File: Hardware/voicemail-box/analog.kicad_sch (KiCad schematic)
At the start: 0 parts

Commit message: ~working on first pcb-Draft
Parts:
- added C25, C26, C29: 10u, Capacitor_SMD:C_0201_0603Metric_Pad0.64x0.40mm_HandSolder, symbol Device:C
- added C27, C28: 1u, Capacitor_SMD:C_0201_0603Metric_Pad0.64x0.40mm_HandSolder, symbol Device:C
- added J2, J7: Conn_02x04_Odd_Even, Connector_PinHeader_2.54mm:PinHeader_2x04_P2.54mm_Vertical, symbol Connector_Generic:Conn_02x04_Odd_Even
- added J3: AudioJack4_SwitchT1, Connector_Audio:Jack_3.5mm_CUI_SJ1-3515N_Horizontal, symbol Connector_Audio:AudioJack4_SwitchT1
- added J4: AudioJack3_Ground, Connector_Audio:Jack_3.5mm_CUI_SJ-3524-SMT_Horizontal, symbol Connector_Audio:AudioJack3_Ground
- added RN4, RN5: 10k, Resistor_SMD:R_Array_Convex_4x0603, symbol Device:R_Pack04
- added U3: PCM5122PW, Package_SO:TSSOP-28_4.4x9.7mm_P0.65mm, symbol Audio:PCM5122PW
- added U4: PCM1809, myParts:WQFN-20-1EP_3x3mm_P0.4mm_EP1.7x1.7mm, symbol myParts:pcm1809
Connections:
- new net: C29.1, U4.17 (AREG)
- new net: C28.1, U4.18 (VREF)
- new net: J2.2 (Pin_2), RN4.5 (R4.2), U4.11 (MD1)
- new net: J2.4 (Pin_4), RN4.6 (R3.2), U4.12 (MD0)
- new net: J2.6 (Pin_6), RN4.7 (R2.2), U4.13 (MSZ)
- new net: J2.8 (Pin_8), RN4.8 (R1.2), U4.19 (FMT0)
- new net: C25.1, U4.14 (DREG)
- new net: C26.1, U4.9 (IOVDD)
- new net: J7.2 (Pin_2), RN5.5 (R4.2), U3.15 (GPIO3/AGNS)
- new net: J7.4 (Pin_4), RN5.6 (R3.2), U3.14 (GPIO4/MAST)
- new net: J7.6 (Pin_6), RN5.7 (R2.2), U3.13 (GPIO5/ATT0)
- new net: J7.8 (Pin_8), RN5.8 (R1.2), U3.19 (GPIO6/FLT)
- new net +3V3: C27.1, RN4.1 (R1.1), RN4.2 (R2.1), RN4.3 (R3.1), RN4.4 (R4.1), RN5.1 (R1.1), RN5.2 (R2.1), RN5.3 (R3.1), RN5.4 (R4.1), U4.16 (AVDD)
- new net ADC_I2S_BCLK: U4.7 (BCLK)
- new net ADC_I2S_FSYNC: U4.8 (FSYNC)
- new net ADC_I2S_SDOUT: U4.6 (SDOUT)
- new net GND: C25.2, C26.2, C27.2, C28.2, C29.2, J2.1 (Pin_1), J2.3 (Pin_3), J2.5 (Pin_5), J2.7 (Pin_7), J7.1 (Pin_1), J7.3 (Pin_3), J7.5 (Pin_5), J7.7 (Pin_7), U4.10 (VSS), U4.15 (VSS), U4.20 (VSS), U4.21 (VSS), U4.5 (VSS)
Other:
- note added: "DAC"
- note added: "Set Jumper for Cntr Signal Low"
- note added: "Signal from Tip Back (Phone Standard): - Left Audio - Right Audio - Ground - Microphone"

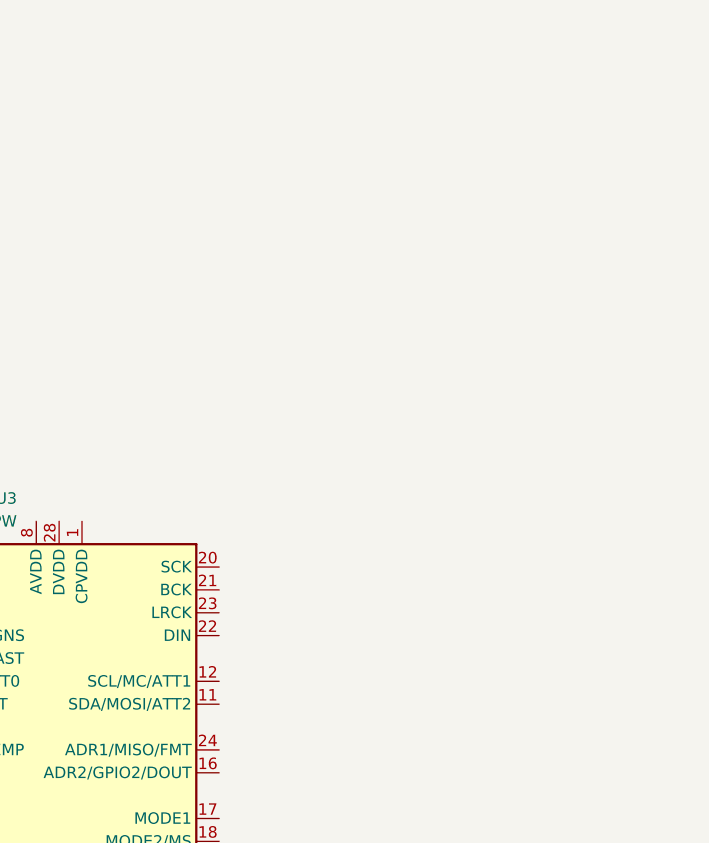
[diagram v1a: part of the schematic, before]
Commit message: - unused datasheets + new datasheets
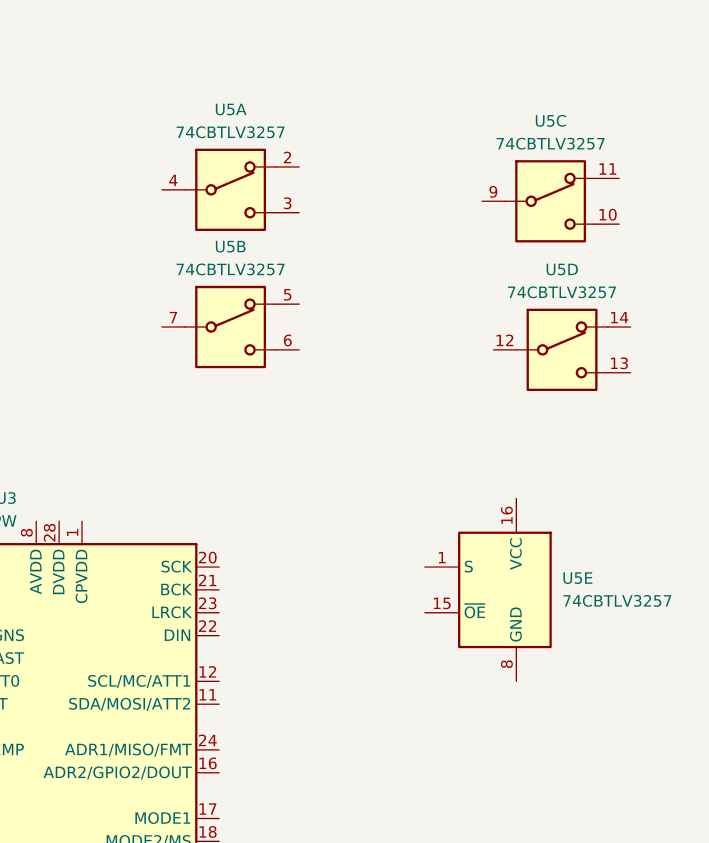
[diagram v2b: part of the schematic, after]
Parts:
- added U5: 74CBTLV3257, symbol 74xx:74CBTLV3257

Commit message: -
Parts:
- removed J2, J7: Conn_02x04_Odd_Even, Connector_PinHeader_2.54mm:PinHeader_2x04_P2.54mm_Vertical, symbol Connector_Generic:Conn_02x04_Odd_Even
- removed RN4, RN5: 10k, Resistor_SMD:R_Array_Convex_4x0603, symbol Device:R_Pack04
- removed U3: PCM5122PW, Package_SO:TSSOP-28_4.4x9.7mm_P0.65mm, symbol Audio:PCM5122PW
- removed U4: PCM1809, myParts:WQFN-20-1EP_3x3mm_P0.4mm_EP1.7x1.7mm, symbol myParts:pcm1809
- removed U5: 74CBTLV3257, symbol 74xx:74CBTLV3257
- added U3: TLV320AIC3104, Package_DFN_QFN:VQFN-32-1EP_5x5mm_P0.5mm_EP3.1x3.1mm, symbol myParts:TLV320AIC3104
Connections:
- net +3V3: no longer C27.1
- net GND: no longer C25.2, C26.2, C27.2, C28.2, C29.2
- new net CODEC_I2C_SCL: U3.8 (SCL)
- new net CODEC_I2C_SDA: U3.9 (SDA)
- new net CODEC_I2S_BCLK: U3.2 (BCLK)
- new net CODEC_I2S_DIN: U3.4 (DIN)
- new net CODEC_I2S_DOUT: U3.5 (DOUT)
- new net CODEC_I2S_MCLK: U3.1 (MCLK)
- new net CODEC_I2S_WCLK: U3.3 (WCLK)
- new net CODEC_nRESET: U3.31 (~{RESET})
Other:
- note removed: "DAC"
- note removed: "Set Jumper for Cntr Signal Low"

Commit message: schematic draft
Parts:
- removed C25, C26, C29: 10u, Capacitor_SMD:C_0201_0603Metric_Pad0.64x0.40mm_HandSolder, symbol Device:C
- removed C28: 1u, Capacitor_SMD:C_0201_0603Metric_Pad0.64x0.40mm_HandSolder, symbol Device:C
- added C601, C603, C605, C608, C612, C613: 100n, Capacitor_SMD:C_0603_1608Metric, symbol Device:C
- added C602, C604, C606, C609: 1u, Capacitor_SMD:C_0603_1608Metric, symbol Device:C
- added C607: 10u, Capacitor_SMD:C_0603_1608Metric, symbol Device:C
- added C610: 100u, Capacitor_SMD:C_0603_1608Metric, symbol Device:C
- added R601, R602: 1k, PCM_4ms_Resistor:R_0603, symbol Device:R
- C611: renamed from C27; value 1u -> 100u; footprint Capacitor_SMD:C_0201_0603Metric_Pad0.64x0.40mm_HandSolder -> Capacitor_SMD:C_0603_1608Metric
- renumbered J4 to J601, J3 to J602, U3 to U601
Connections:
- net +3V3: now also U601.24 (DRVDD), U601.25 (AVDD), U601.7 (IOVDD), C601.2, C602.2, C605.2, C606.2, C607.2, C608.2, C609.2
- net GND: now also U601.17 (AVSS1), U601.21 (DRVSS), U601.26 (AVSS2), U601.33 (DRVSS), U601.6 (DVSS), C601.1, C602.1, C603.1, C604.1, C605.1, C606.1, C607.1, C608.1, C609.1, R602.2
- net at C611.1: now also U601.23 (HPROUT23)
- net at U601.19 (HPLOUT23): now also C610.1
- net +1V8: now reaches U601.32 (DVDD)
- net +1V8: now also C603.2, C604.2
- net at U601.10 (MIC1LP): now also C612.1
- net at U601.11 (MIC1LM): now also C613.1
- net micbias: now reaches U601.15 (MICBIAS)
- net micbias: now also R601.1
- new net: C612.2, R601.2
- new net: C613.2, R602.1
- no-connect marks 0 -> 19
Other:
- note added: "Standard for 3.5mm Jack unclear... Output driver for owr situation needed"
- moved on the sheet: C611, J601, J602, U601A, U601B, U601D

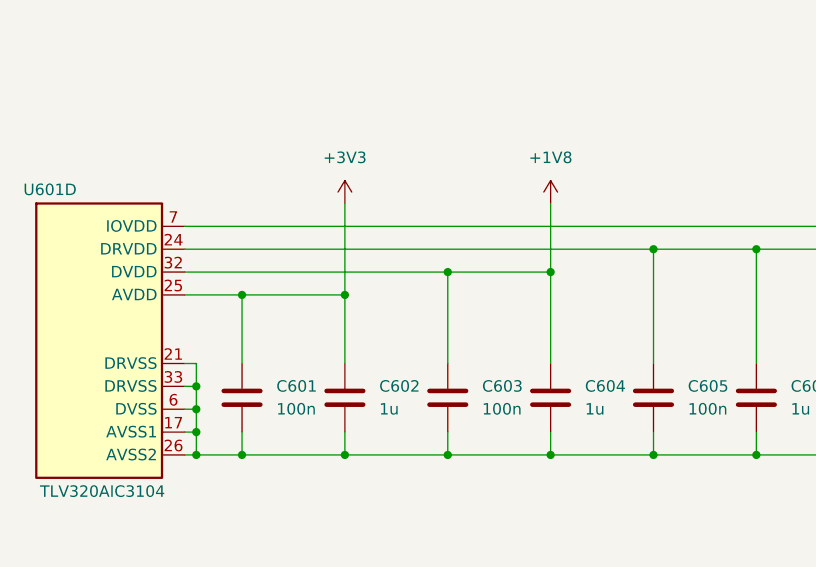
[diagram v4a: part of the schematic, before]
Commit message: HW Layout progress todo: + Antenna + Audio Jacks + Planes (Supply only)
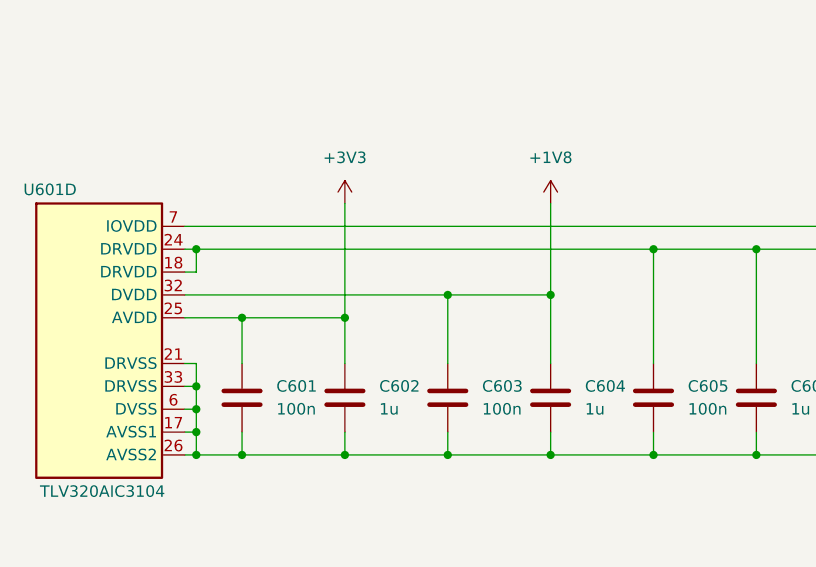
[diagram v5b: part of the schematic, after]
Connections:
- net +3V3: now also U601.18 (DRVDD)
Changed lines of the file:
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@@
+	)
+	(junction
+		(at 44.45 132.08)
+		(diameter 0)
+		(color 0 0 0 0)
 	)
 	(junction
@@
 	)
 	(junction
-		(at 67.31 147.32)
+		(at 55.88 132.08)
 		(diameter 0)
 		(color 0 0 0 0)
 	)
 	(junction
-		(at 44.45 129.54)
-		(diameter 0)
-		(color 0 0 0 0)
-	)
-	(junction
-		(at 78.74 127)
+		(at 67.31 147.32)
 		(diameter 0)
 		(color 0 0 0 0)
@@
 	)
 	(junction
+		(at 39.37 124.46)
+		(diameter 0)
+		(color 0 0 0 0)
+	)
+	(junction
 		(at 39.37 147.32)
 		(diameter 0)
@@
 	)
 	(junction
-		(at 67.31 127)
-		(diameter 0)
-		(color 0 0 0 0)
-	)
-	(junction
 		(at 113.03 124.46)
 		(diameter 0)
@@
 	)
 	(junction
-		(at 55.88 129.54)
+		(at 78.74 129.54)
+		(diameter 0)
+		(color 0 0 0 0)
+	)
+	(junction
+		(at 67.31 129.54)
 		(diameter 0)
 		(color 0 0 0 0)
@@
 	(wire
 		(pts
-			(xy 67.31 137.16) (xy 67.31 127)
+			(xy 67.31 137.16) (xy 67.31 129.54)
 		)
 		(stroke
@@
 	(wire
 		(pts
-			(xy 44.45 137.16) (xy 44.45 129.54)
+			(xy 44.45 137.16) (xy 44.45 132.08)
 		)
 		(stroke
@@
 	(wire
 		(pts
+			(xy 39.37 124.46) (xy 90.17 124.46)
+		)
+		(stroke
+			(width 0)
+			(type default)
+		)
+	)
+	(wire
+		(pts
 			(xy 168.91 64.77) (xy 168.91 63.5)
 		)
@@
 	(wire
 		(pts
-			(xy 78.74 119.38) (xy 78.74 127)
+			(xy 78.74 119.38) (xy 78.74 129.54)
 		)
 		(stroke
@@
 	(wire
 		(pts
+			(xy 39.37 127) (xy 39.37 124.46)
+		)
+		(stroke
+			(width 0)
+			(type default)
+		)
+	)
+	(wire
+		(pts
+			(xy 55.88 132.08) (xy 55.88 137.16)
+		)
+		(stroke
+			(width 0)
+			(type default)
+		)
+	)
+	(wire
+		(pts
 			(xy 55.88 144.78) (xy 55.88 147.32)
 		)
@@
 	(wire
 		(pts
-			(xy 78.74 137.16) (xy 78.74 127)
+			(xy 78.74 137.16) (xy 78.74 129.54)
 		)
 		(stroke
@@
 	(wire
 		(pts
+			(xy 38.1 127) (xy 39.37 127)
+		)
+		(stroke
+			(width 0)
+			(type default)
+		)
+	)
+	(wire
+		(pts
 			(xy 135.89 137.16) (xy 135.89 121.92)
 		)
@@
 	(wire
 		(pts
-			(xy 55.88 129.54) (xy 55.88 137.16)
-		)
-		(stroke
-			(width 0)
-			(type default)
-		)
-	)
-	(wire
-		(pts
 			(xy 39.37 147.32) (xy 39.37 144.78)
 		)
@@
 	(wire
 		(pts
+			(xy 55.88 119.38) (xy 55.88 132.08)
+		)
+		(stroke
+			(width 0)
+			(type default)
+		)
+	)
+	(wire
+		(pts
 			(xy 154.94 67.31) (xy 158.75 67.31)
 		)
@@
 	(wire
 		(pts
-			(xy 44.45 129.54) (xy 55.88 129.54)
+			(xy 44.45 132.08) (xy 55.88 132.08)
 		)
 		(stroke
@@
 	(wire
 		(pts
-			(xy 38.1 124.46) (xy 90.17 124.46)
+			(xy 38.1 124.46) (xy 39.37 124.46)
 		)
 		(stroke
@@
 	(wire
 		(pts
-			(xy 78.74 127) (xy 67.31 127)
+			(xy 78.74 129.54) (xy 67.31 129.54)
 		)
 		(stroke
@@
 	(wire
 		(pts
-			(xy 55.88 119.38) (xy 55.88 129.54)
-		)
-		(stroke
-			(width 0)
-			(type default)
-		)
-	)
-	(wire
-		(pts
 			(xy 44.45 147.32) (xy 55.88 147.32)
 		)
@@
 	(wire
 		(pts
-			(xy 67.31 127) (xy 38.1 127)
+			(xy 67.31 129.54) (xy 38.1 129.54)
 		)
 		(stroke
@@
 	(wire
 		(pts
-			(xy 44.45 129.54) (xy 38.1 129.54)
+			(xy 44.45 132.08) (xy 38.1 132.08)
 		)
 		(stroke
@@
 		(pin "1"
 		)
+		(pin "18"
+		)
 		(instances
 			(project ""
@@
 		(pin "1"
 		)
+		(pin "18"
+		)
 		(instances
 			(project ""
@@
 		)
 		(pin "1"
+		)
+		(pin "18"
 		)
 		(instances
@@
 		(pin "1"
 		)
+		(pin "18"
+		)
 		(instances

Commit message: schema review
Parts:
- removed J601: AudioJack3_Ground, Connector_Audio:Jack_3.5mm_CUI_SJ-3524-SMT_Horizontal, symbol Connector_Audio:AudioJack3_Ground
- removed J602: AudioJack4_SwitchT1, Connector_Audio:Jack_3.5mm_CUI_SJ1-3515N_Horizontal, symbol Connector_Audio:AudioJack4_SwitchT1
- added C614, C615, C620: np, Capacitor_SMD:C_0603_1608Metric_Pad1.08x0.95mm_HandSolder, symbol Device:C
- added C616, C617, C618, C619: 47n, Capacitor_SMD:C_0603_1608Metric_Pad1.08x0.95mm_HandSolder, symbol Device:C
- added J601: Conn_02x02_Odd_Even, Connector_PinHeader_2.54mm:PinHeader_2x02_P2.54mm_Vertical, symbol Connector_Generic:Conn_02x02_Odd_Even
- added J602, J605: AudioJack3_SwitchTR, Connector_Audio:Jack_3.5mm_CUI_SJ2-3593D-SMT_Horizontal, symbol Connector_Audio:AudioJack3_SwitchTR
- added J603: Phoenix 1844236, Connector_Phoenix_MC:PhoenixContact_MC_1,5_4-G-3.5_1x04_P3.50mm_Horizontal, symbol Connector_Generic:Conn_01x04
- added J604: Conn_01x03, Connector_PinHeader_2.54mm:PinHeader_1x03_P2.54mm_Vertical, symbol Connector_Generic:Conn_01x03
- added MK601: MD9745APZ-F, Connector_PinHeader_2.54mm:PinHeader_1x02_P2.54mm_Vertical, symbol Device:Microphone
- added R603: 100k, Resistor_SMD:R_0603_1608Metric_Pad0.98x0.95mm_HandSolder, symbol Device:R
- added R604, R605, R606, R607: 100R, Resistor_SMD:R_0603_1608Metric_Pad0.98x0.95mm_HandSolder, symbol Device:R
- added R608, R609: np, Resistor_SMD:R_0603_1608Metric_Pad0.98x0.95mm_HandSolder, symbol Device:R
- added R610, R611: 0R, Resistor_SMD:R_0603_1608Metric_Pad0.98x0.95mm_HandSolder, symbol Device:R
- added SW601: CTS 218-4LPSTR, Package_SO:SSOP-8_3.9x5.05mm_P1.27mm, symbol Switch:SW_DIP_x04
- C602, C604, C609: value 1u -> 10u
- R601, R602: value 1k -> 2k2; footprint PCM_4ms_Resistor:R_0603 -> Resistor_SMD:R_0603_1608Metric_Pad0.98x0.95mm_HandSolder
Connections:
- net +3V3: now also J604.1 (Pin_1), R603.1
- net CODEC_nRESET: now also R603.2
- net GND: now also C614.2, C615.2, C616.2, C617.2, C618.2, C619.2, C620.2, J605.S, MK601.1 (-), R608.2, R609.2, SW601.4; no longer R602.2
- net micbias: now also C620.1, J604.3 (Pin_3); no longer R601.1
- net at C611.1, U601.23 (HPROUT23): now also SW601.2
- net at C611.2: now also J602.T, SW601.7
- net at C610.1, U601.19 (HPLOUT23): now also SW601.1
- net at U601.20 (HPLCOM): now also R611.1
- net at U601.22 (HPRCOM): now also R610.1
- net at U601.27 (LLOP): now also R604.1
- net at U601.28 (LLOM): now also R605.1
- net at U601.29 (RLOP): now also R606.1
- net at U601.30 (RLOM): now also R607.1
- net at C612.2, R601.2: now also J605.T, R608.1
- net at C613.1: now also U601.16 (MIC2R), C614.1; no longer U601.11 (MIC1LM)
- net at C613.2: now also R602.2, J605.R, R609.1; no longer R602.1
- net at U601.10 (MIC1LP): no longer C612.1
- net at U601.14 (MIC2L): now also C612.1, C615.1
- net at C610.2: now also J602.R, SW601.8
- new net: R610.2, R611.2, SW601.3
- new net: J602.S, SW601.5, SW601.6
- new net: J601.2 (Pin_2), J601.4 (Pin_4), MK601.2 (+)
- new net: J604.2 (Pin_2), R601.1, R602.1
- new net: J601.1 (Pin_1), J605.RN
- new net: J601.3 (Pin_3), J605.TN
- new net Left+: C619.1, J603.1 (Pin_1), R604.2
- new net Left-: C618.1, J603.2 (Pin_2), R605.2
- new net Right+: C617.1, J603.3 (Pin_3), R606.2
- new net Right-: C616.1, J603.4 (Pin_4), R607.2
- no-connect marks 19 -> 6
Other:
- note added: "Headphone"
- note added: "Microphone ext"
- note added: "Microphone on Board"
- note added: "Speaker"
- note removed: "Signal from Tip Back (Phone Standard): - Left Audio - Right Audio - Ground - Microphone"
- note removed: "Standard for 3.5mm Jack unclear... Output driver for owr situation needed"
- moved on the sheet: C601, C602, C603, C604, C605, C606, C607, C608, C609, C610, C611, C612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

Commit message: ~layout
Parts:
- added C621: 100n, Capacitor_SMD:C_0603_1608Metric_Pad1.08x0.95mm_HandSolder, symbol Device:C
- added C622: 1u, Capacitor_SMD:C_0603_1608Metric_Pad1.08x0.95mm_HandSolder, symbol Device:C
- added U602: MAX98306xDT, Package_DFN_QFN:TDFN-14-1EP_3x3mm_P0.4mm_EP1.78x2.35mm, symbol Amplifier_Audio:MAX98306xDT
- C601, C602, C603, C604, C605, C606, C607, C608, C609, C612, C613: footprint Capacitor_SMD:C_0603_1608Metric -> Capacitor_SMD:C_0603_1608Metric_Pad1.08x0.95mm_HandSolder
- C610, C611: footprint Capacitor_SMD:C_0603_1608Metric -> Capacitor_SMD:C_0805_2012Metric_Pad1.18x1.45mm_HandSolder
- MK601: value MD9745APZ-F -> CMA-4544PF-W
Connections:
- net GND: now also C621.1, C622.1, U602.1 (PGND), U602.15 (PGND), U602.8 (PGND)
- net Left+: now also U602.3 (INL+); no longer J603.1 (Pin_1)
- net Left-: now also U602.4 (INL-); no longer J603.2 (Pin_2)
- net Right+: now also U602.7 (INR+); no longer J603.3 (Pin_3)
- net Right-: now also U602.6 (INR-); no longer J603.4 (Pin_4)
- net at C611.2, SW601.7: now also J602.R; no longer J602.T
- net at C610.2, SW601.8: now also J602.T; no longer J602.R
- new net: J603.3 (Pin_3), U602.10 (OUTR+)
- new net: J603.1 (Pin_1), U602.13 (OUTL+)
- new net: J603.2 (Pin_2), U602.14 (OUTL-)
- new net: J603.4 (Pin_4), U602.9 (OUTR-)
- new net +5V: C621.2, C622.2, U602.11 (PVDD), U602.12 (PVDD), U602.2 (~{SHDN}), U602.5 (GAIN)
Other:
- moved on the sheet: C610, C611, C616, C617, C618, C619, J602, J603, J604, MK601, R601, R602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
